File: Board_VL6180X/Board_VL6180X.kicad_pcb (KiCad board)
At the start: 2 copper layers, 15 x 16 mm, 12 parts, among them J1 Conn_01x06, U1 VL53L0X

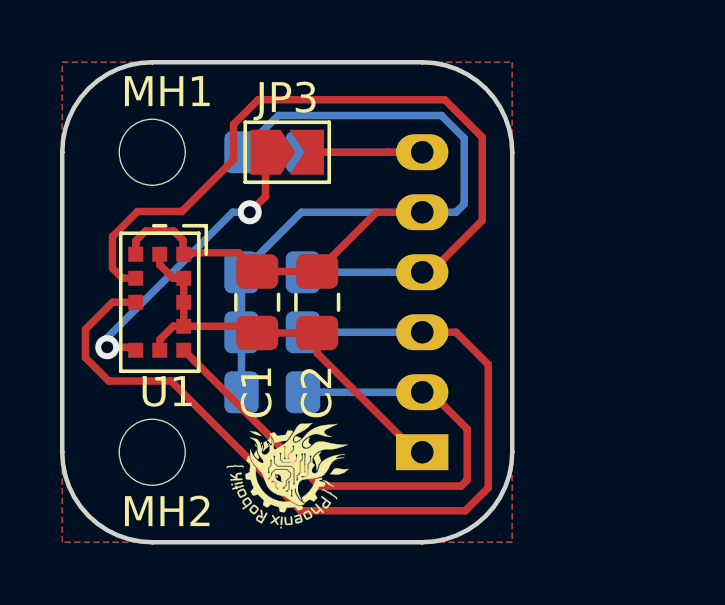
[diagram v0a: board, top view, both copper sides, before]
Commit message: PCB VL6180X done
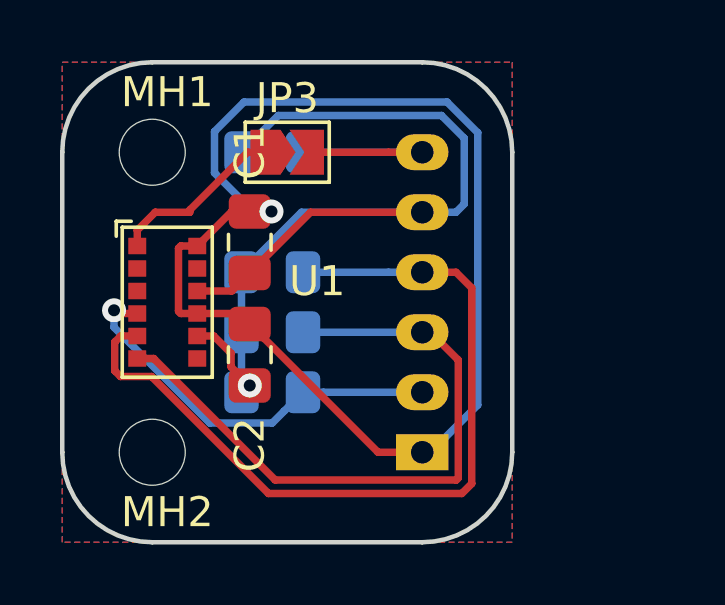
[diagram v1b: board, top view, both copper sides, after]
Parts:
- removed REF**: Logo_5,1mm, PhoenixRobotik:Logo_5,1mm
- R3, R4: value 10k -> 47k
- U1: value VL53L0X -> VL6180X; footprint PhoenixRobotik:TOF-12_4.4x2.4x1.0mm_P0.8mm -> PhoenixRobotik:ST_LGA-12_2.8x4.8x1.0mm_P0.75mm
- moved C2 2.85 mm to (106.2, 89.8)
- moved C1 2.02 mm to (106.2, 86.0), turned to 90 degrees
- moved U1 0.25 mm to (103.5, 88.0), turned to 0 degrees
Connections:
- C2 pad 1: +2V8 -> GND
- C2 pad 2: GND -> +2V8
- U1 pad 1: +2V8 -> Net-(JP3-Pad1)
- U1 pad 2: /I2C_SDA -> (no net)
- U1 pad 3: /I2C_SCL -> (no net)
- U1 pad 4: GND -> /~XSHUT
- U1 pad 5: /~XSHUT -> /I2C_SCL
- U1 pad 6: Net-(JP3-Pad1) -> /I2C_SDA
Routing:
- net GND: track 14.4 -> 41.0 mm, vias 0 -> 1
- net /I2C_SDA: track 29.6 -> 21.9 mm
- net /~XSHUT: track 19.1 -> 13.4 mm, vias 0 -> 1
- net Net-(JP3-Pad1): track 10.0 -> 5.92 mm, vias 2 -> 0
- net /I2C_SCL: track 26.9 -> 27.9 mm
- net +2V8: track 34.6 -> 34.1 mm, vias 0 -> 1

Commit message: Changed JST connectors
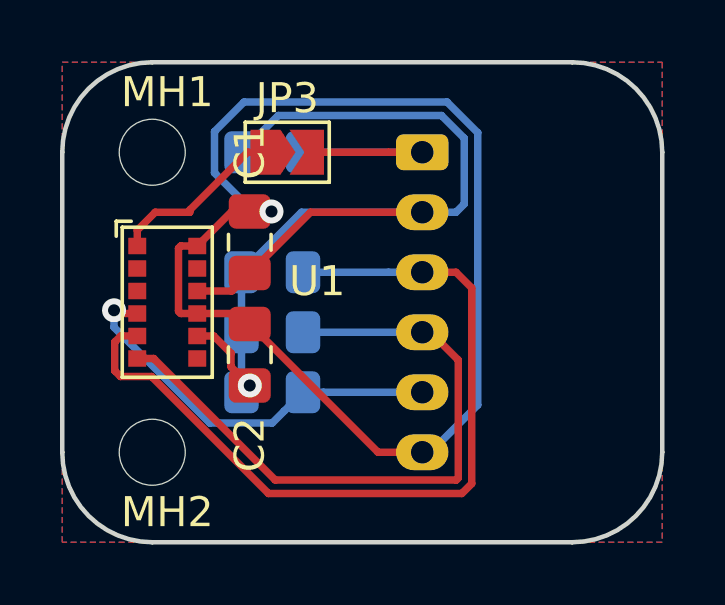
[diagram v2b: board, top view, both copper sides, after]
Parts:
- J1: footprint Connector_JST:JST_PH_B6B-PH-K_1x06_P2.00mm_Vertical -> Connector_JST:JST_PH_S6B-PH-K_1x06_P2.00mm_Horizontal
- moved J1 10.0 mm to (112.0, 83.0), turned to 270 degrees
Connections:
- J1 pad 1: GND -> /GPIO
- J1 pad 2: /~XSHUT -> +2V8
- J1 pad 3: /I2C_SDA -> /I2C_SCL
- J1 pad 4: /I2C_SCL -> /I2C_SDA
- J1 pad 5: +2V8 -> /~XSHUT
- J1 pad 6: /GPIO -> GND
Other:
- board size 15 x 16 mm -> 20 x 16 mm

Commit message: update board
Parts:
- MH1, MH2: value MountingHole -> MountingHole_Pad; footprint MountingHole:MountingHole_2.2mm_M2 -> MountingHole:MountingHole_2.2mm_M2_Pad
- R1, R2, R3, R4: moved to F.Cu
- U1: footprint PhoenixRobotik:ST_LGA-12_2.8x4.8x1.0mm_P0.75mm -> PhenixRobotik:ST_LGA-12_2.8x4.8x1.0mm_P0.75mm
- moved J1 11.5 mm to (117.6, 93.0), turned to 90 degrees
- moved JP3 10.4 mm to (109.4, 93.2)
- moved R4 10.3 mm to (112.4, 91.8), turned to 270 degrees
- moved R2 7.67 mm to (114.4, 89.0), turned to 90 degrees
- moved R3 7.33 mm to (110.2, 84.4), turned to 90 degrees
- moved R1 5.49 mm to (112.4, 88.0), turned to 270 degrees
- moved C1 4.37 mm to (108.0, 90.0), turned to 270 degrees
- moved C2 3.96 mm to (110.2, 90.0), turned to 90 degrees
- moved U1 0.50 mm to (103.0, 88.0), turned to 180 degrees
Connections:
- MH1 pad 1: (no net) -> GND
- MH2 pad 1: (no net) -> GND
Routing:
- net GND: track 40.8 -> 7.53 mm, vias 1 -> 2
- net /I2C_SCL: track 27.9 -> 14.5 mm
- net +2V8: track 34.1 -> 25.4 mm, vias 1 -> 4
- net /I2C_SDA: track 21.9 -> 14.0 mm
- net /~XSHUT: track 13.4 -> 16.0 mm, vias 1 -> 2

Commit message: add logos
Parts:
- added LOGO1: Logo_Open_Hardware_Small, Symbol:OSHW-Logo2_7.3x6mm_SilkScreen, B.Cu at (107.8, 92.6)
- added LOGO2: Logo_Open_Hardware_Small, PhenixRobotik:Logo_8,5mm, B.Cu at (107.6, 84.6)
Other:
- board text removed: "+2V8"
- board text removed: "GND"

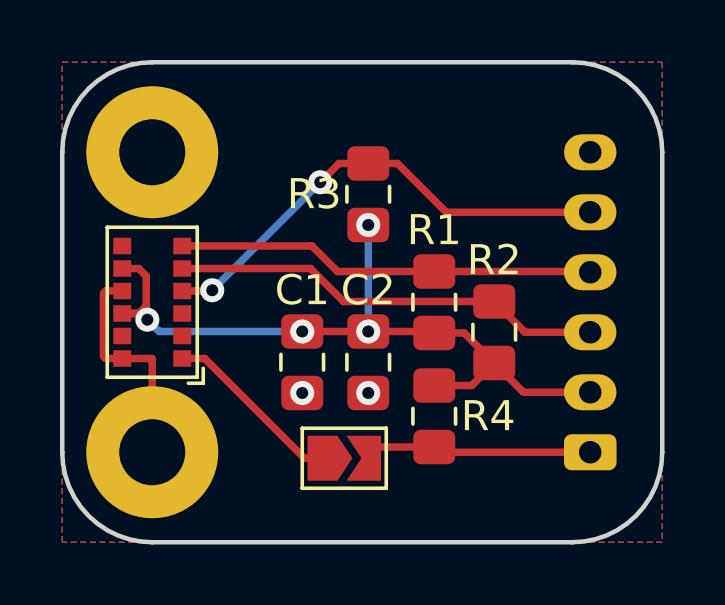
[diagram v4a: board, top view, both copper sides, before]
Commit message: Changed connector orientation, better capacitance positionning, cleaner pcb
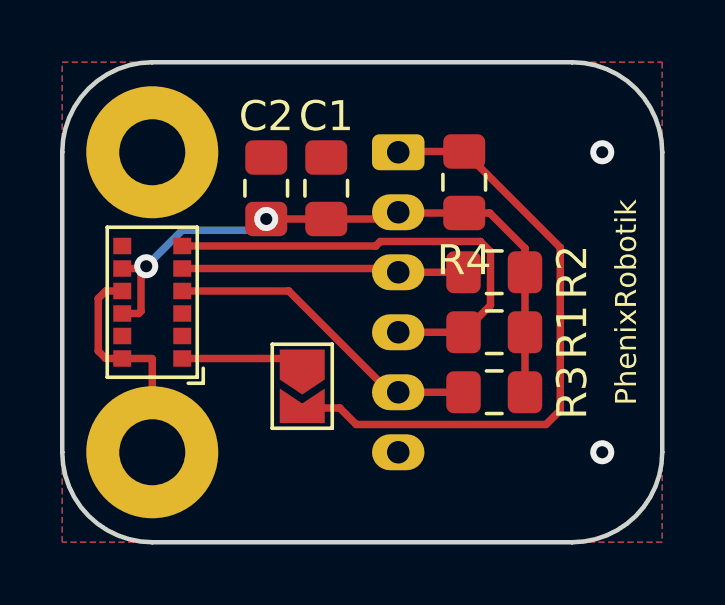
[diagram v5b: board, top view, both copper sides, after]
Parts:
- moved J1 11.9 mm to (111.2, 83.0), turned to 270 degrees
- moved R4 7.86 mm to (113.4, 84.0), turned to 90 degrees
- moved R3 7.82 mm to (114.4, 91.0), turned to 180 degrees
- moved C2 6.72 mm to (106.8, 84.2), turned to 270 degrees
- moved C1 5.85 mm to (108.8, 84.2), turned to 90 degrees
- moved LOGO2 3.03 mm to (107.2, 87.6)
- moved JP3 2.78 mm to (108.0, 90.8), turned to 270 degrees
- moved R1 2.24 mm to (114.4, 89.0), turned to 0 degrees
- moved R2 2.00 mm to (114.4, 87.0), turned to 180 degrees
- moved LOGO1 0.60 mm to (107.8, 93.2)
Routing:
- net /GPIO: track 7.70 -> 21.2 mm
- net /~XSHUT: track 16.0 -> 10.8 mm, vias 2 -> 0
- net /I2C_SCL: track 14.5 -> 9.43 mm
- net +2V8: track 25.4 -> 21.6 mm, vias 4 -> 2
- net Net-(JP3-Pad1): track 6.05 -> 4.08 mm
- net /I2C_SDA: track 14.0 -> 15.7 mm
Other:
- board text added: "PhenixRobotik"
